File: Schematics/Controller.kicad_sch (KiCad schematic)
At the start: 37 parts, among them IC1 F280049CPMSR, J17 43650-0418, J18 43650-0418, J19 FTSH-105-01-LM-D-K, J20 43045-1212, Q7 PC817X1CSP9F, Y1 ABM8-20.000MHZ-B2-T

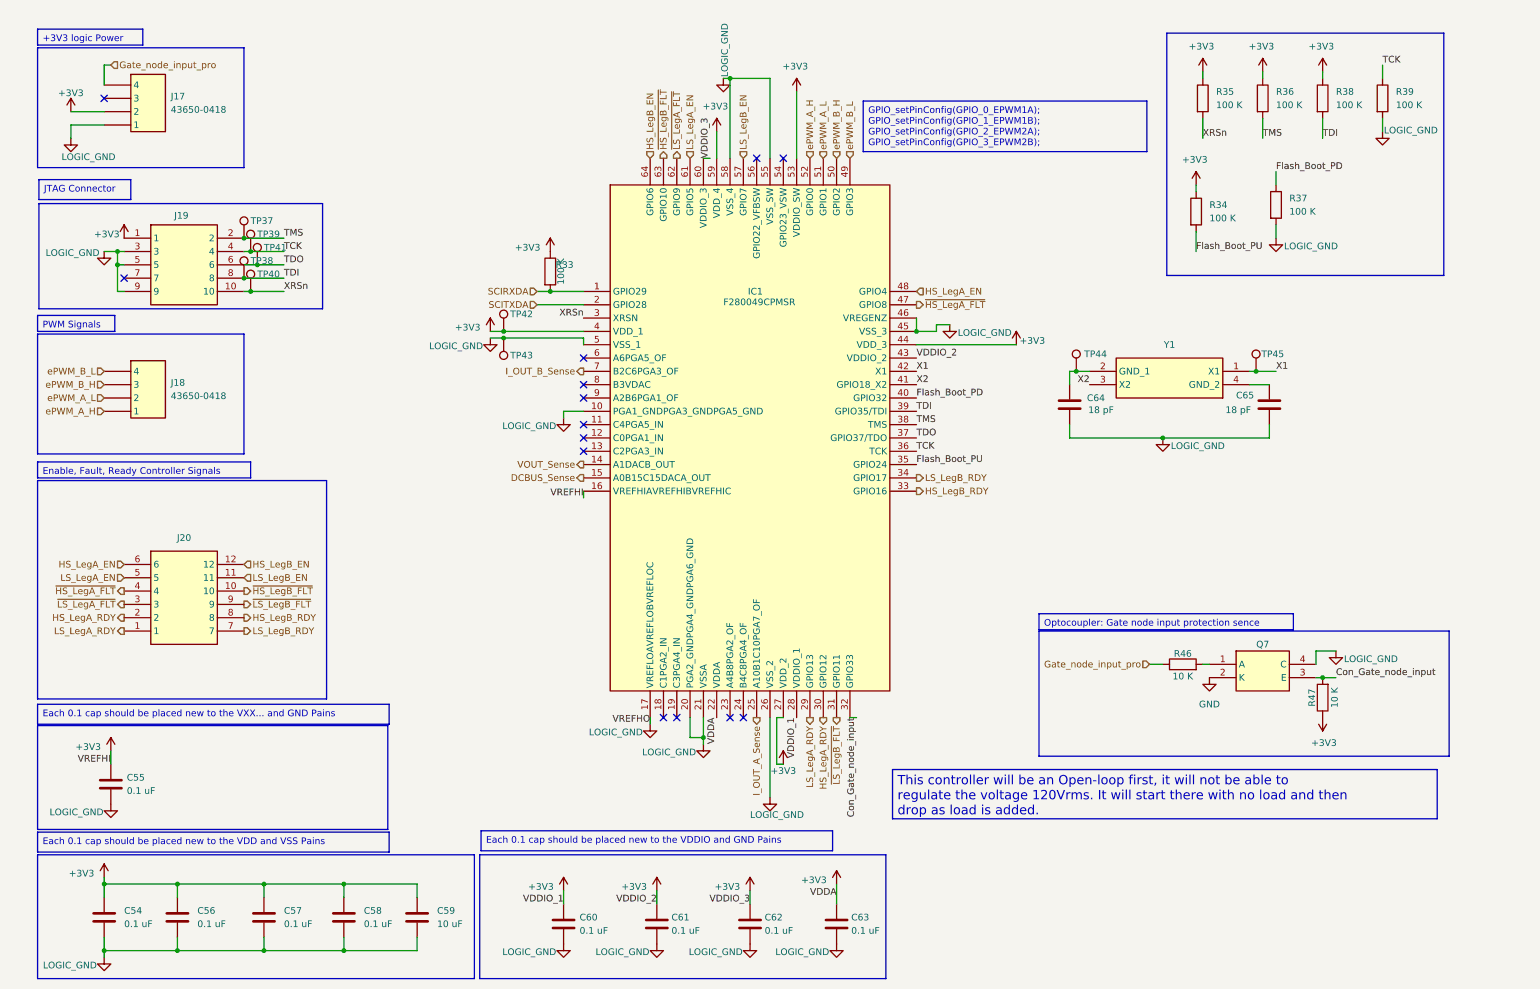
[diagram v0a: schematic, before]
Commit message: Added Precharge Gate Driver to controller and per charge sub circuit
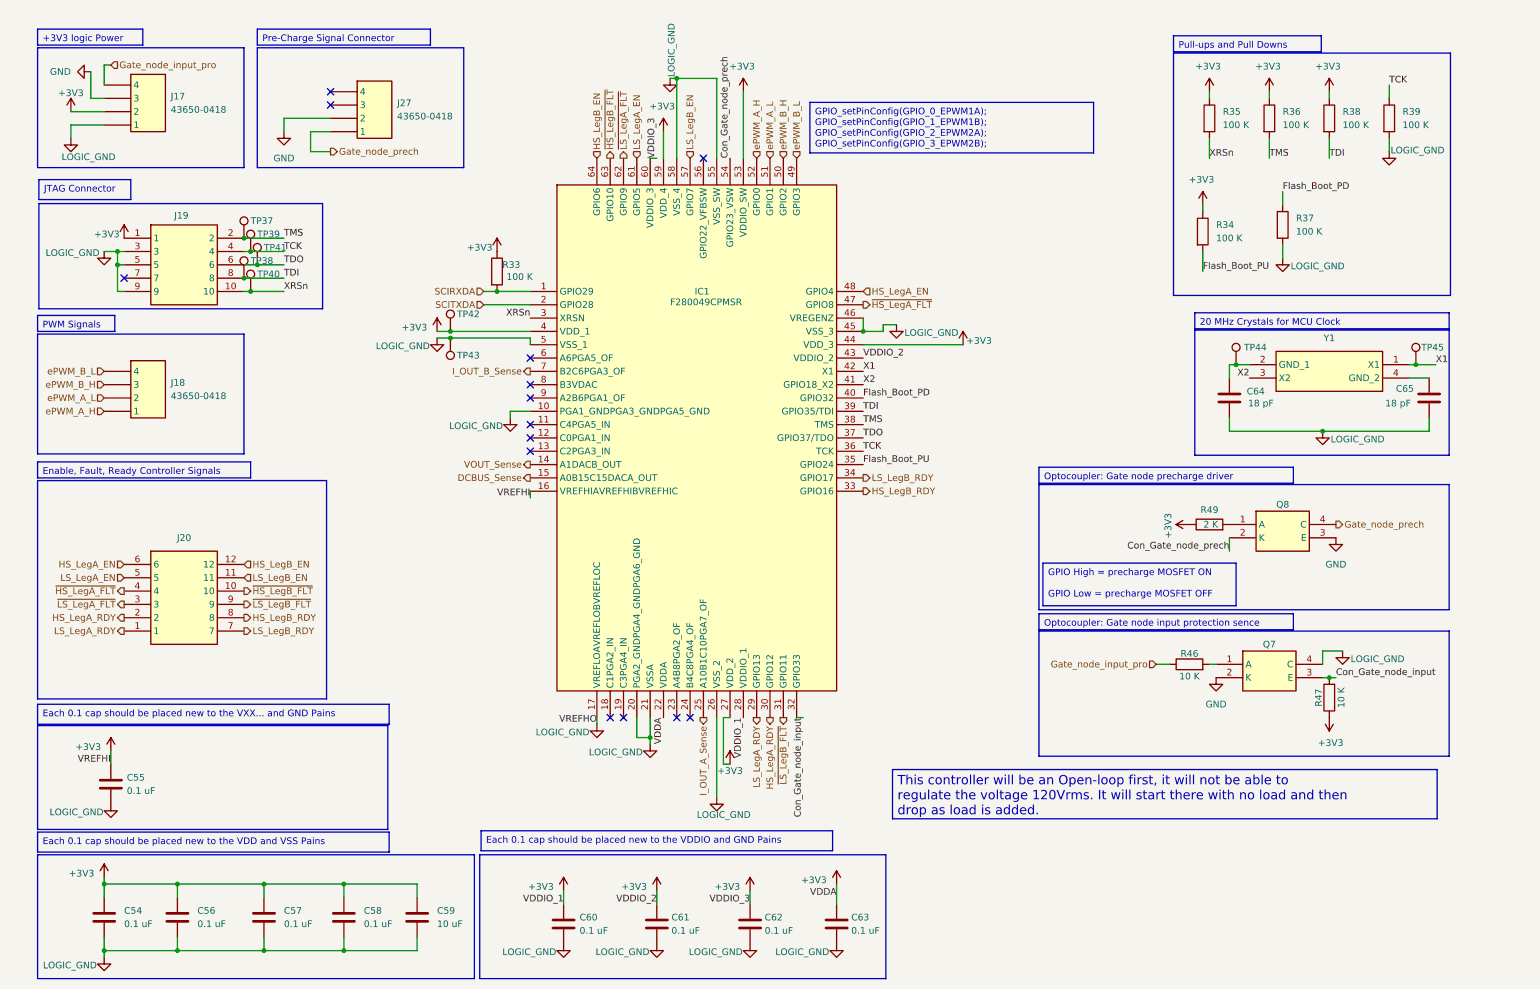
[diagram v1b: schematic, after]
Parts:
- added J27: 43650-0418, SiC_Inverter:436500418, symbol SiC_Inverter:43650-0418
- added Q8: PC817X1CSP9F, SiC_Inverter:PC817X1CSP9F, symbol SiC_Inverter:PC817X1CSP9F
- added R49: 2 K, Resistor_SMD:R_1206_3216Metric_Pad1.30x1.75mm_HandSolder, symbol SiC_Inverter:RT1206BRD072KL
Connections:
- net +3V3: now also R49.1
- net GND: now also J17.3, J27.2, Q8.3 (E)
- net Con_Gate_node_prech: now reaches IC1.54 (GPIO23_VSW)
- net Con_Gate_node_prech: now also Q8.2 (K)
- new net: Q8.1 (A), R49.2
- new net Gate_node_prech: J27.1, Q8.4 (C)
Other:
- moved on the sheet: C64, C65, IC1, Q7, R33, R34, R35, R36, R37, R38, R39, R46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

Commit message: WIP PCB, Added Test Points, added icon file
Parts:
- removed TP43: 5281, SiC_Inverter:5281, symbol SiC_Inverter:5281
- added TP38, TP40, TP41, TP43, TP44, TP45, TP46, TP47, TP48, TP49, TP50, TP56, TP57, TP58, TP60, TP61, TP62, TP63, TP65: 5277, SiC_Inverter:5277, symbol SiC_Inverter:5277
- added TP39, TP59: 5281, SiC_Inverter:5281, symbol SiC_Inverter:5281
- renumbered J17 to J18, J18 to J21, J27 to J22, Q7 to Q6, Q8 to Q7, R33 to R34, R46 to R35, R34 to R36, R35 to R37, R49 to R38, R36 to R39, R37 to R40, R38 to R41, R47 to R42, R39 to R43, TP37 to TP51, TP41 to TP52, TP40 to TP53, TP39 to TP54, TP38 to TP55, TP44 to TP64, TP45 to TP66
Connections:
- net +3V3: now also TP38.1; no longer TP42.1
- net Con_Gate_node_input: now also TP65.1
- net GND: now also TP59.1
- net Gate_node_input_pro: now also TP40.1
- net Gate_node_prech: now also TP63.1
- net HS_LegA_EN: now also TP43.1
- net HS_LegA_RDY: now also TP45.1
- net HS_LegB_EN: now also TP56.1
- net HS_LegB_RDY: now also TP58.1
- net LOGIC_GND: now also TP39.1
- net LS_LegA_EN: now also TP48.1
- net LS_LegA_RDY: now also TP50.1
- net LS_LegB_EN: now also TP60.1
- net LS_LegB_RDY: now also TP62.1
- net ePWM_A_H: now also TP47.1
- net ePWM_A_L: now also TP42.1
- net ePWM_B_H: now also TP46.1
- net ePWM_B_L: now also TP41.1
- net ~{HS_LegA_FLT}: now also TP44.1
- net ~{HS_LegB_FLT}: now also TP57.1
- net ~{LS_LegA_FLT}: now also TP49.1
- net ~{LS_LegB_FLT}: now also TP61.1
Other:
- moved on the sheet: J21, TP51, TP52, TP53, TP54, TP55, TP64

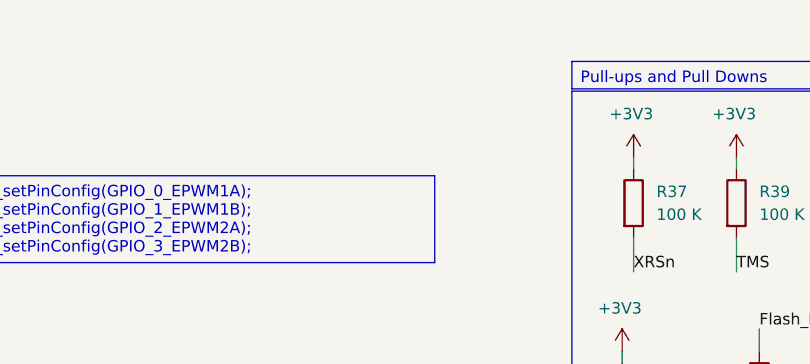
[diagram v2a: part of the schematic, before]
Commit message: Adding Damping Resiter to AC Output Filter and mounting points
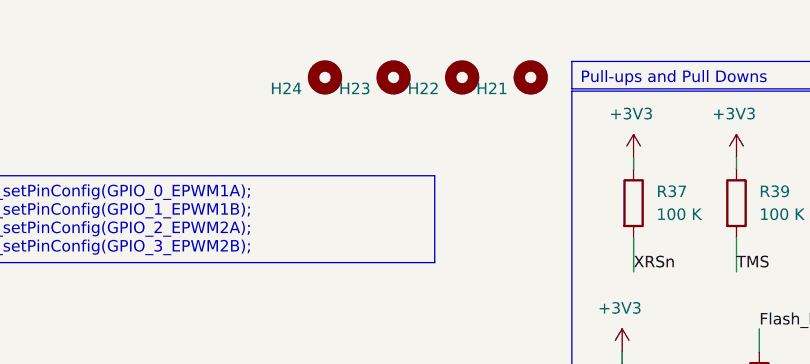
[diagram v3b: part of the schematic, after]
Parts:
- added H21, H22, H23, H24: MountingHole, MountingHole:MountingHole_2.2mm_M2, symbol Mechanical:MountingHole

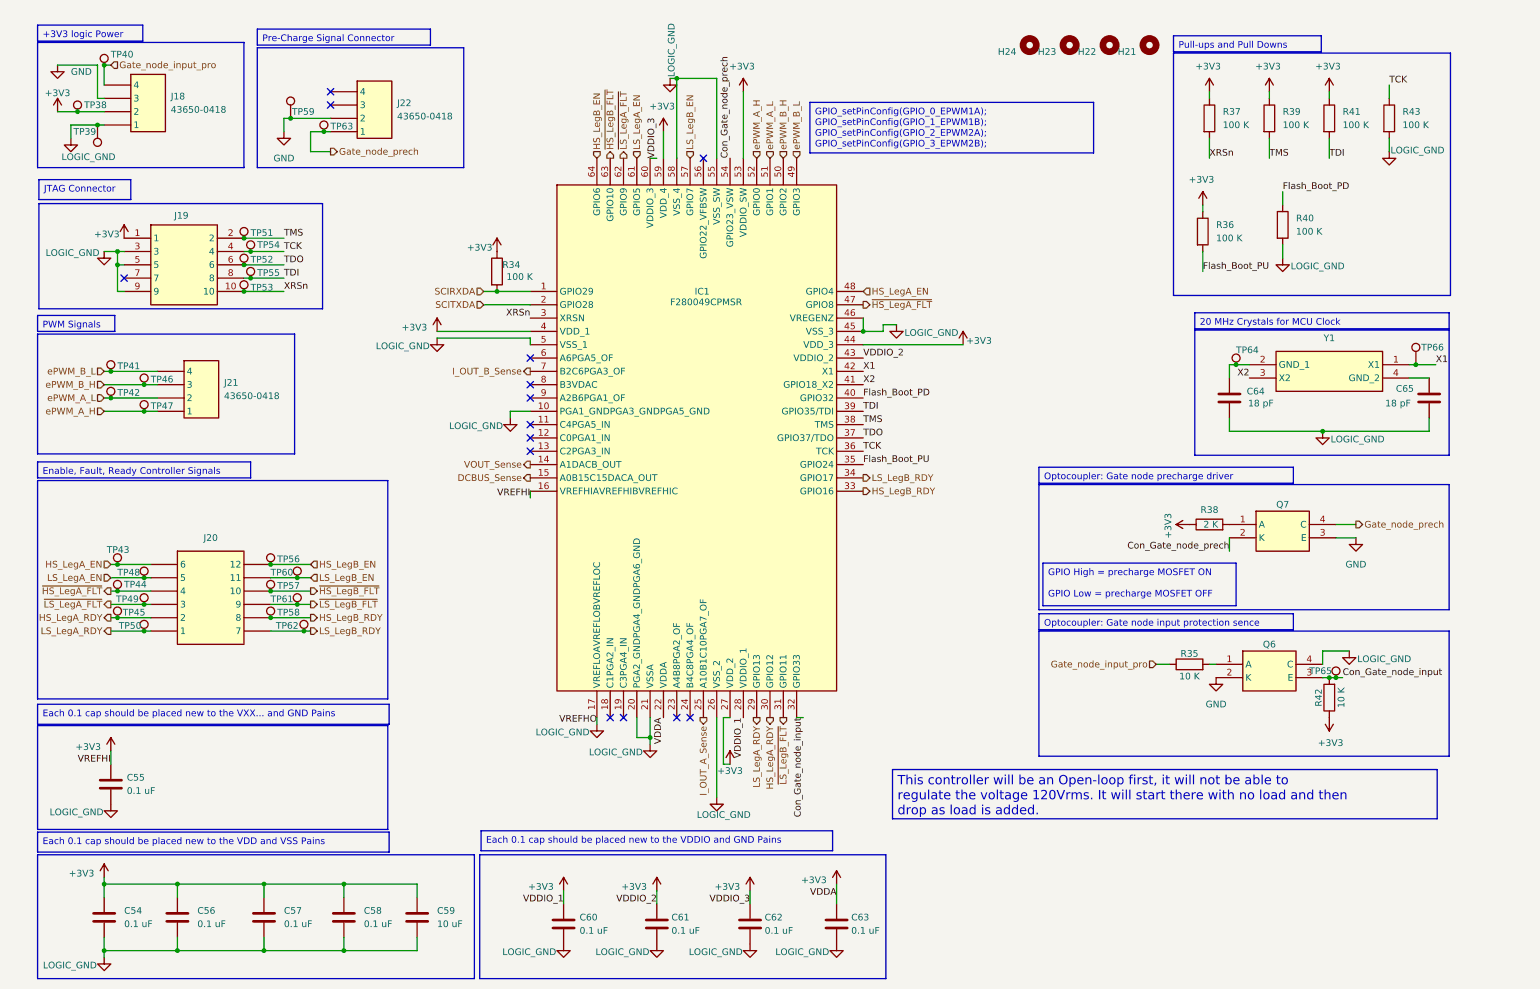
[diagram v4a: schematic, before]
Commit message: WIP PCB Design Controller
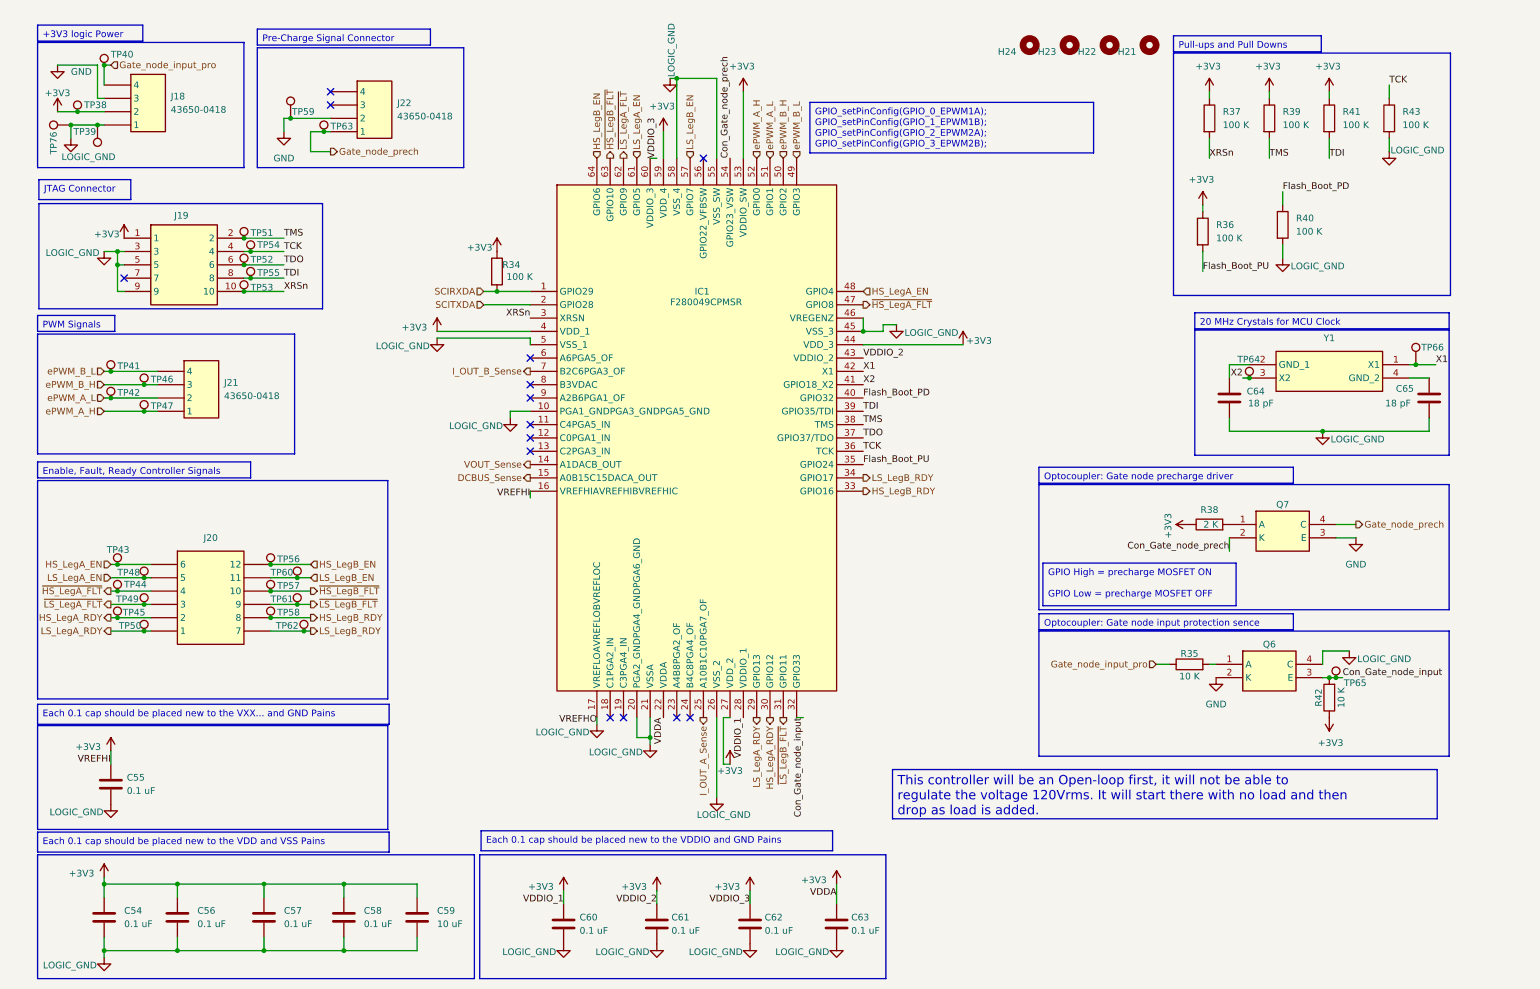
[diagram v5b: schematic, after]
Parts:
- added TP76: 5281, SiC_Inverter:5281, symbol SiC_Inverter:5281
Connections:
- net LOGIC_GND: now also TP76.1
- net X2: now also TP64.1
- net at C64.1, Y1.2 (GND_1): no longer TP64.1
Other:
- moved on the sheet: TP64
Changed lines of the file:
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@@
 	)
 	(junction
+		(at 20.32 33.02)
+		(diameter 0)
+		(color 0 0 0 0)
+	)
+	(junction
 		(at 29.21 121.92)
 		(diameter 0)
@@
 	)
 	(junction
-		(at 242.57 78.74)
+		(at 63.5 119.38)
 		(diameter 0)
 		(color 0 0 0 0)
 	)
 	(junction
-		(at 63.5 119.38)
+		(at 53.34 59.69)
 		(diameter 0)
 		(color 0 0 0 0)
 	)
 	(junction
-		(at 53.34 59.69)
+		(at 54.61 57.15)
 		(diameter 0)
 		(color 0 0 0 0)
 	)
 	(junction
-		(at 54.61 57.15)
+		(at 245.11 81.28)
 		(diameter 0)
 		(color 0 0 0 0)
@@
 	(wire
 		(pts
-			(xy 242.57 78.74) (xy 245.11 78.74)
+			(xy 241.3 78.74) (xy 245.11 78.74)
 		)
 		(stroke
@@
 	(wire
 		(pts
+			(xy 243.84 81.28) (xy 245.11 81.28)
+		)
+		(stroke
+			(width 0)
+			(type default)
+		)
+	)
+	(wire
+		(pts
 			(xy 53.34 57.15) (xy 54.61 57.15)
 		)
@@
 	(wire
 		(pts
-			(xy 241.3 78.74) (xy 242.57 78.74)
-		)
-		(stroke
-			(width 0)
-			(type default)
-		)
-	)
-	(wire
-		(pts
 			(xy 66.04 121.92) (xy 58.42 121.92)
 		)
@@
 	)
 	(label "X2"
-		(at 245.11 81.28 180)
+		(at 243.84 81.28 180)
 		(effects
 			(font
@@
 	(symbol
 		(lib_id "SiC_Inverter:5277")
-		(at 242.57 80.01 0)
+		(at 245.11 82.55 0)
 		(unit 1)
 		(body_style 1)
@@
 		(dnp no)
 		(property "Reference" "TP64"
-			(at 246.888 75.946 0)
+			(at 247.142 77.724 0)
 			(show_name no)
 			(do_not_autoplace no)
@@
 		)
 		(property "Value" "5277"
-			(at 226.568 92.964 0)
+			(at 229.108 95.504 0)
 			(hide yes)
 			(show_name no)
@@
 		)
 		(property "Footprint" "SiC_Inverter:5277"
-			(at 232.664 91.186 0)
+			(at 235.204 93.726 0)
 			(hide yes)
 			(show_name no)
@@
 		)
 		(property "Datasheet" "https://www.keyelco.com/userAssets/file/K75p62.pdf"
-			(at 250.444 87.376 0)
+			(at 252.984 89.916 0)
 			(hide yes)
 			(show_name no)
@@
 		)
 		(property "Description" "Test Plugs & Test Jacks TEST POINT (BLUE) - COMPACT"
-			(at 252.984 89.408 0)
+			(at 255.524 91.948 0)
 			(hide yes)
 			(show_name no)
@@
 		(dnp no)
 		(property "Reference" "TP65"
-			(at 260.858 137.16 0)
+			(at 267.462 139.446 0)
 			(show_name no)
 			(do_not_autoplace no)
@@
 					(unit 1)
 				)
+			)
+		)
+	)
+	(symbol
+		(lib_id "SiC_Inverter:5281")
+		(at 20.32 33.02 90)
+		(unit 1)
+		(body_style 1)
+		(exclude_from_sim no)
+		(in_bom yes)
+		(on_board yes)
+		(in_pos_files yes)
+		(dnp no)
+		(property "Reference" "TP76"
+			(at 17.018 38.608 0)
+			(show_name no)
+			(do_not_autoplace no)
+			(effects
+				(font
+					(size 1.27 1.27)
+				)
+				(justify left)
+			)
+		)
+		(property "Value" "5281"
+			(at 33.274 49.022 0)
+			(hide yes)
+			(show_name no)
+			(do_not_autoplace no)
+			(effects
+				(font
+					(size 1.27 1.27)
+				)
+			)
+		)
+		(property "Footprint" "SiC_Inverter:5281"
+			(at 31.496 42.926 0)
+			(hide yes)
+			(show_name no)
+			(do_not_autoplace no)
+			(effects
+				(font
+					(size 1.27 1.27)
+				)
+			)
+		)
+		(property "Datasheet" "https://www.keyelco.com/userAssets/file/K75p62.pdf"
+			(at 27.686 25.146 0)
+			(hide yes)
+			(show_name no)
+			(do_not_autoplace no)
+			(effects
+				(font
+					(size 1.27 1.27)
+				)
+			)
+		)
+		(property "Description" "Test Plugs & Test Jacks TEST POINT BLACK MULTIPURPOSE"
+			(at 29.718 22.606 0)
+			(hide yes)
+			(show_name no)
+			(do_not_autoplace no)
+			(effects
+				(font
+					(size 1.27 1.27)
+				)
+			)
+		)
+		(pin "1"
+		)
+		(instances
+			(project "SiC_Single_Phase_Inverter"
+				(path "/a1ed0539-9735-4ad1-a8fd-87e26e7fce16/7e4e3ba0-41da-43fa-8607-bd1c726f4bc0"
+					(reference "TP76")
+					(unit 1)
+				)
